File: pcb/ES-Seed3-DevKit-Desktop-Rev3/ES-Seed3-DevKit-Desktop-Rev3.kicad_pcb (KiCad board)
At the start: 2 copper layers, 197 x 111 mm, 244 parts, among them J1 AudioJack3_Switch, J10 DIN_MIDI_5P, J11 DIN_MIDI_5P, J2 AudioJack3_Switch, J3 AudioJack3_Switch, J4 AudioJack3_Switch, J5 AudioJack3_Switch_HEADPHONE, J7 USB4110GFA, J8 DIN_MIDI_5P, Q1 MMBT3904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

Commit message: schematic level changes for fixing CV idle offset, and audio whine tone.
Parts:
- removed D21, D22, D23, D24: 1N5817WS, Diode_SMD:D_SOD-323F
- removed R64, R65: 47K, Resistor_SMD:R_0603_1608Metric
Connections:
- J_CV_IN_1 pad NORM: unconnected-(J_CV_IN_1-PadNORM) -> GND
- J_CV_IN_2 pad NORM: unconnected-(J_CV_IN_2-PadNORM) -> GND
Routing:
- net +3V3_A: track 214.9 -> 190.9 mm, vias 6 -> 4
- net CODEC_IN_R: track 153.0 -> 149.3 mm
- net CODEC_IN_L: track 162.5 -> 159.0 mm

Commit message: initial changes made. need feedback on silk screen.
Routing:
- net Net-(C9-Pad1): track 5.42 -> 3.82 mm
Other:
- board text added: "A: D28 B: D27"
- board text added: "CD4021 CLK: D8 LATCH: D9 DATA: D10"
- board text added: "D0"
- board text added: "D13"
- board text added: "D14"
- board text added: "D18"
- board text added: "D19"
- board text added: "D20"
- board text added: "D21"
- board text added: "D22"
- board text added: "D23"
- board text added: "Detect: D7"
- board text added: "Mux 4051: ADC: D15 CTRL A: D24 CTRL B: D25 CTRL C: D26"
- board text added: "PCA9685: I2C1 SCL: D11 SCK: D12 ADDR: 0x00"
- board text added: "Plug Detect: Left: D16 Right: D17"
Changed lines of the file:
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@@
 		(tags "capacitor")
 		(property "Reference" "C6"
-			(at 2.54 0 0)
+			(at -0.02625 1.7125 0)
 			(layer "F.SilkS")
 			(effects
@@
 		(tags "resistor")
 		(property "Reference" "R57"
-			(at 0 -3.175 0)
+			(at 3.23375 -0.11625 0)
 			(layer "F.SilkS")
 			(effects
@@
 		(tags "resistor")
 		(property "Reference" "R60"
-			(at -3.175 0 90)
+			(at -0.16375 1.72625 90)
 			(layer "F.SilkS")
 			(effects
@@
 		(tags "resistor")
 		(property "Reference" "R56"
-			(at 0 3.175 0)
+			(at -3.23375 0.11625 0)
 			(layer "F.SilkS")
 			(effects
@@
 		(tags "neutrik jack m")
 		(property "Reference" "J2"
-			(at 6.35 -3 90)
+			(at -6.265 -3.035 90)
 			(layer "F.SilkS")
 			(effects
@@
 		(descr "<b>TF-01A-6</b><br>")
 		(property "Reference" "MICRO_SD7"
-			(at 4.8 -9.325 270)
+			(at 0.05 -9.475 270)
 			(layer "F.SilkS")
 			(effects
@@
 		)
 	)
+	(gr_text "D21"
+		(at 161 81.5 0)
+		(layer "F.SilkS")
+		(effects
+			(font
+				(size 1 1)
+				(thickness 0.15)
+			)
+			(justify right bottom)
+		)
+	)
+	(gr_text "D23"
+		(at 130.5 66 0)
+		(layer "F.SilkS")
+		(effects
+			(font
+				(size 1 1)
+				(thickness 0.15)
+			)
+			(justify right bottom)
+		)
+	)
 	(gr_text "AUDIO\nIN RIGHT"
 		(at 189.6 75.2 0)
@@
 		)
 	)
+	(gr_text "D22"
+		(at 130.25 81.5 0)
+		(layer "F.SilkS")
+		(effects
+			(font
+				(size 1 1)
+				(thickness 0.15)
+			)
+			(justify right bottom)
+		)
+	)
+	(gr_text "Mux 4051:\nADC: D15\nCTRL A: D24\nCTRL B: D25\nCTRL C: D26"
+		(at 144 93 0)
+		(layer "F.SilkS")
+		(effects
+			(font
+				(size 1 1)
+				(thickness 0.15)
+			)
+			(justify right bottom)
+		)
+	)
 	(gr_text "INPUT"
 		(at 229.4 122.5 90)
@@
 		)
 	)
+	(gr_text "D14"
+		(at 238 124 0)
+		(layer "F.SilkS")
+		(effects
+			(font
+				(size 1 1)
+				(thickness 0.15)
+			)
+			(justify right bottom)
+		)
+	)
 	(gr_text "OUT"
 		(at 229.2 67.9 90)
@@
 		)
 	)
+	(gr_text "PCA9685:\nI2C1\nSCL: D11\nSCK: D12\nADDR: 0x00"
+		(at 123 119 0)
+		(layer "F.SilkS")
+		(effects
+			(font
+				(size 1 1)
+				(thickness 0.15)
+			)
+			(justify right bottom)
+		)
+	)
+	(gr_text "D20"
+		(at 161 66 0)
+		(layer "F.SilkS")
+		(effects
+			(font
+				(size 1 1)
+				(thickness 0.15)
+			)
+			(justify right bottom)
+		)
+	)
 	(gr_text "ON-OFF-ON"
 		(at 81.915 148.59 0)
@@
 		)
 	)
+	(gr_text "CD4021\nCLK: D8\nLATCH: D9\nDATA: D10"
+		(at 100 134 0)
+		(layer "F.SilkS")
+		(effects
+			(font
+				(size 1 1)
+				(thickness 0.15)
+			)
+			(justify right bottom)
+		)
+	)
+	(gr_text "D19"
+		(at 95 151 0)
+		(layer "F.SilkS")
+		(effects
+			(font
+				(size 1 1)
+				(thickness 0.15)
+			)
+			(justify bottom)
+		)
+	)
+	(gr_text "A: D28\nB: D27"
+		(at 82 152 0)
+		(layer "F.SilkS")
+		(effects
+			(font
+				(size 1 1)
+				(thickness 0.15)
+			)
+			(justify bottom)
+		)
+	)
+	(gr_text "D18"
+		(at 171 81.5 0)
+		(layer "F.SilkS")
+		(effects
+			(font
+				(size 1 1)
+				(thickness 0.15)
+			)
+			(justify right bottom)
+		)
+	)
+	(gr_text "Plug Detect:\nLeft: D16\nRight: D17"
+		(at 233.25 50 0)
+		(layer "F.SilkS")
+		(effects
+			(font
+				(size 1 1)
+				(thickness 0.15)
+			)
+			(justify right bottom)
+		)
+	)
 	(gr_text "Get Started Here!"
 		(at 57.256572 59.196 0)
@@
 		)
 	)
+	(gr_text "D13"
+		(at 226.75 66.25 0)
+		(layer "F.SilkS")
+		(effects
+			(font
+				(size 1 1)
+				(thickness 0.15)
+			)
+			(justify right bottom)
+		)
+	)
+	(gr_text "D0"
+		(at 171 66 0)
+		(layer "F.SilkS")
+		(effects
+			(font
+				(size 1 1)
+				(thickness 0.15)
+			)
+			(justify right bottom)
+		)
+	)
+	(gr_text "Detect: D7"
+		(at 66 144.25 0)
+		(layer "F.SilkS")
+		(effects
+			(font
+				(size 1 1)
+				(thickness 0.15)
+			)
+			(justify left bottom)
+		)
+	)
 	(gr_text "AUDIO\nIN LEFT"
 		(at 212.8 75.2 0)
@@
 	)
 	(segment
-		(start 193 80.425)
-		(end 194.6 80.425)
-		(width 0.254)
-		(layer "F.Cu")
-		(net 44)
-	)
-	(segment

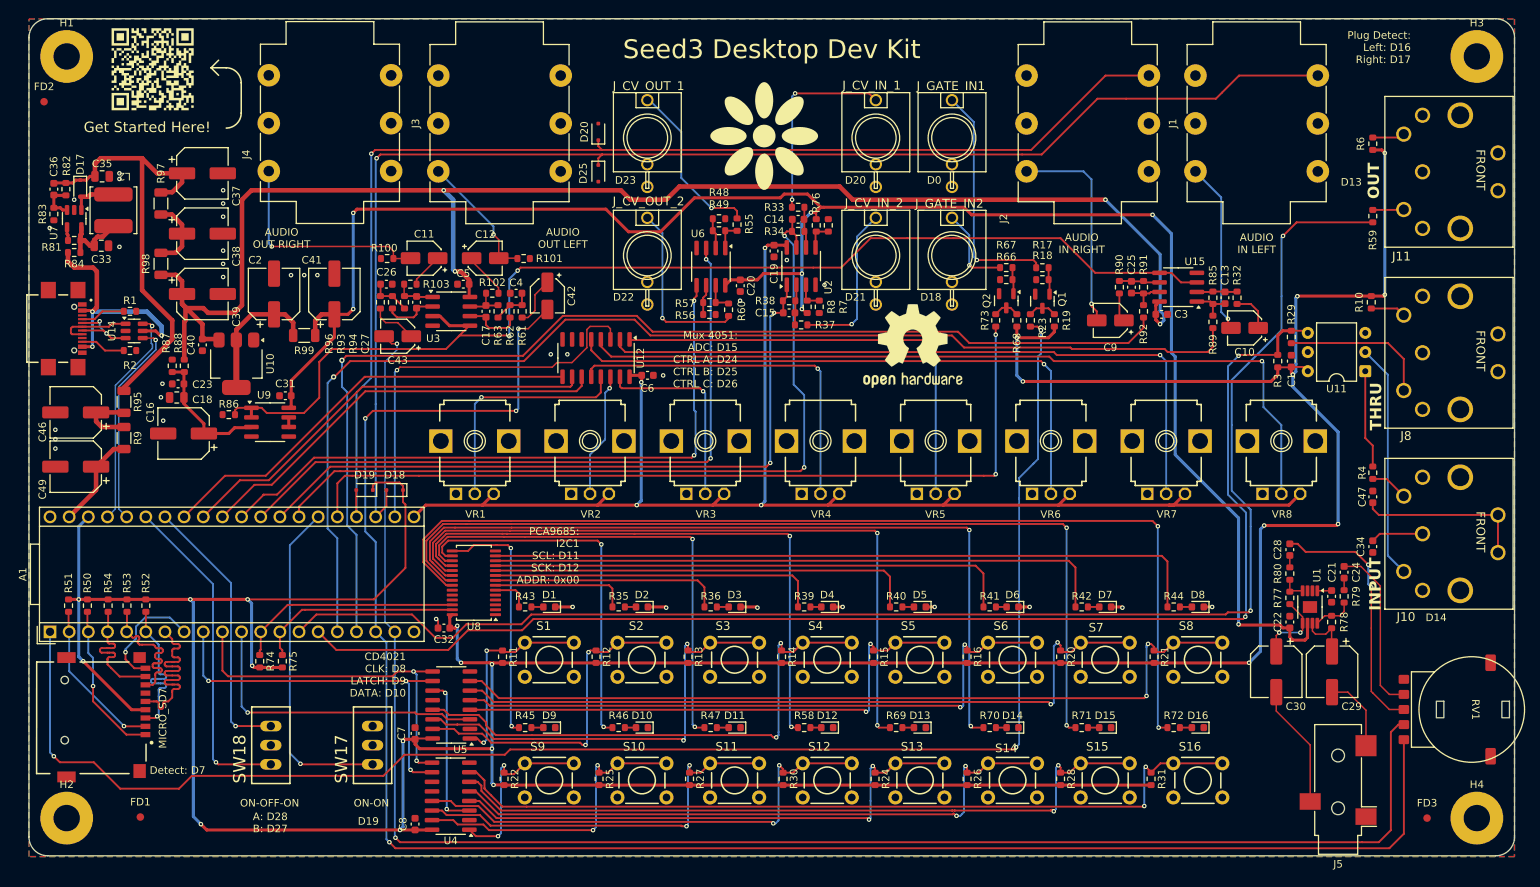
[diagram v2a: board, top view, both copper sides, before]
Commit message: updated changelog with rev3 changes, updated silkscreen for software pin mappings, and swapped DAC channels so the STM32 ch matches the names on the PCB.
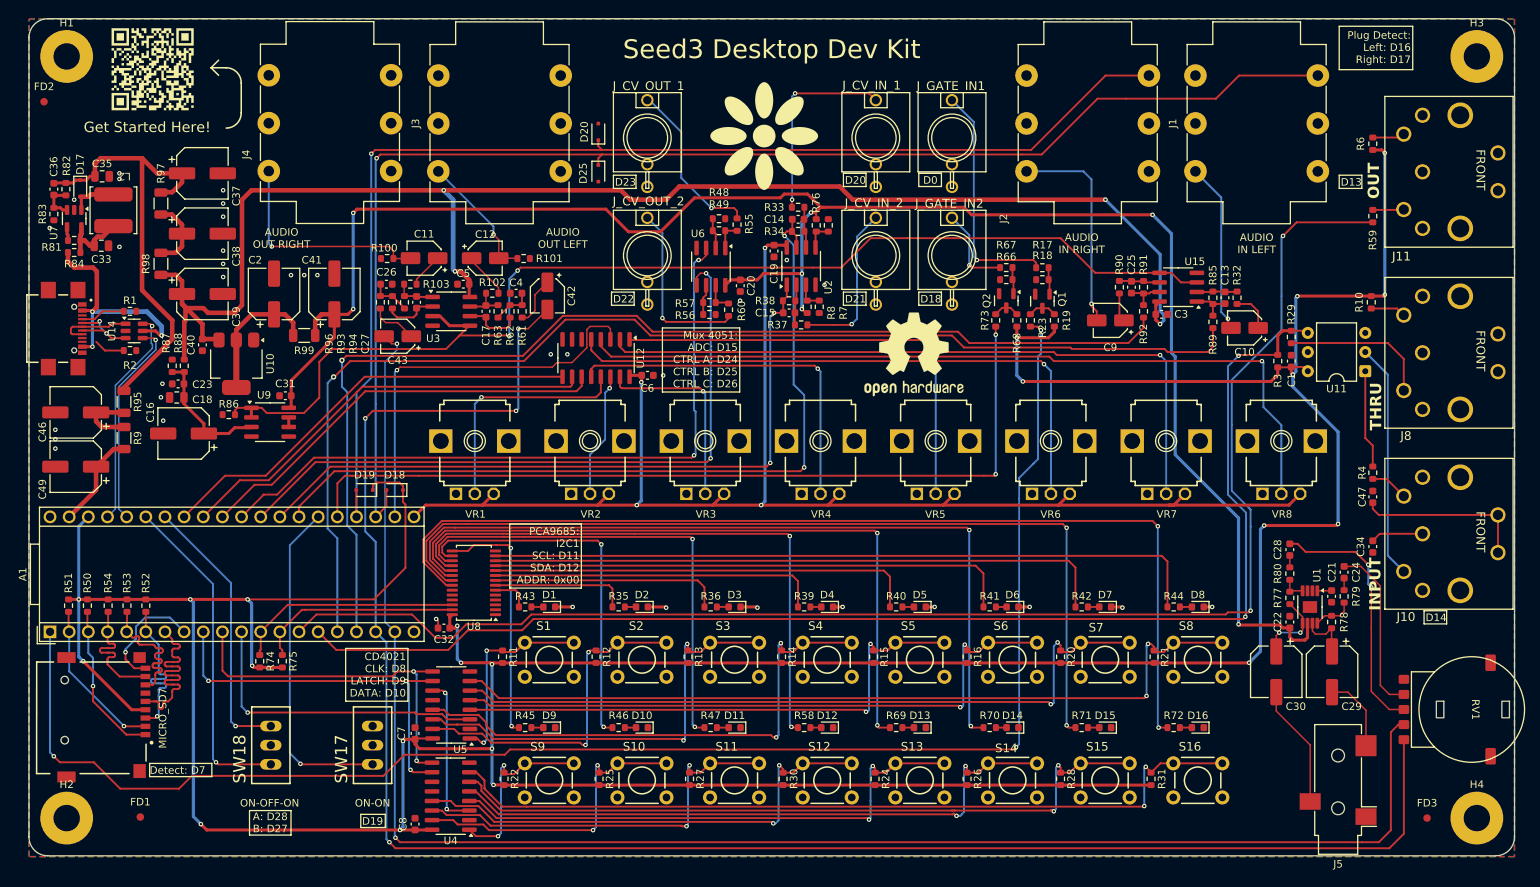
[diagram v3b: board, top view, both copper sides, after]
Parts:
- moved LOGO1 1.11 mm to (167.3, 88.5)
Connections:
- A1 pad 29: /Daisy/DAC_CV_1 -> /Daisy/DAC_CV_2
- A1 pad 30: /Daisy/DAC_CV_2 -> /Daisy/DAC_CV_1
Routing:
- net /Daisy/DAC_CV_2: track 86.3 -> 90.2 mm
- net Net-(J7-CC2): track 5.98 -> 4.13 mm
- net /Daisy/DAC_CV_1: track 91.0 -> 92.1 mm
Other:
- board text added: "PCA9685: I2C1 SCL: D11 SDA: D12 ADDR: 0x00"
- board text removed: "PCA9685: I2C1 SCL: D11 SCK: D12 ADDR: 0x00"
